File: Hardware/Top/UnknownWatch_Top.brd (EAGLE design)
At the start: 38 x 38 mm, 49 parts, among them U2 NRF52832_MODULE_MDBT42, U4 PCF8523

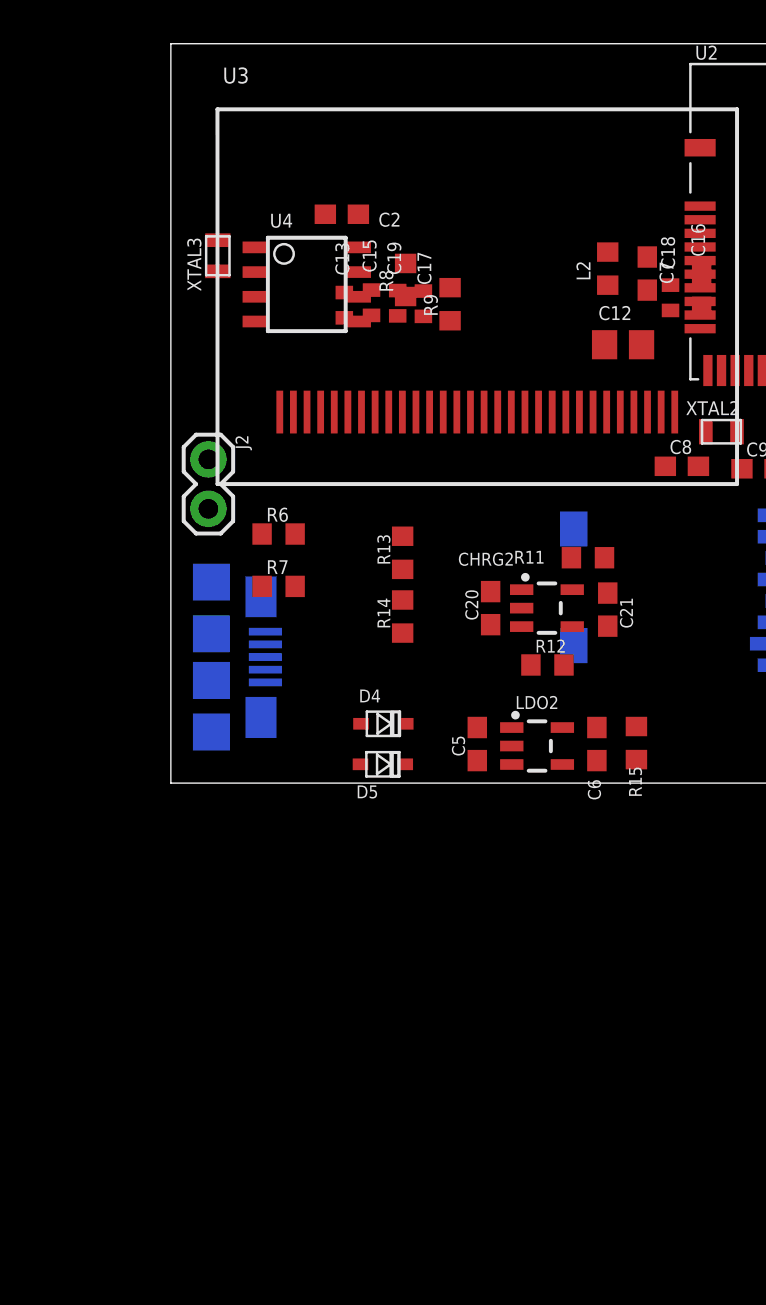
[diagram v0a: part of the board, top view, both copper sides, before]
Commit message: Adde Buttons
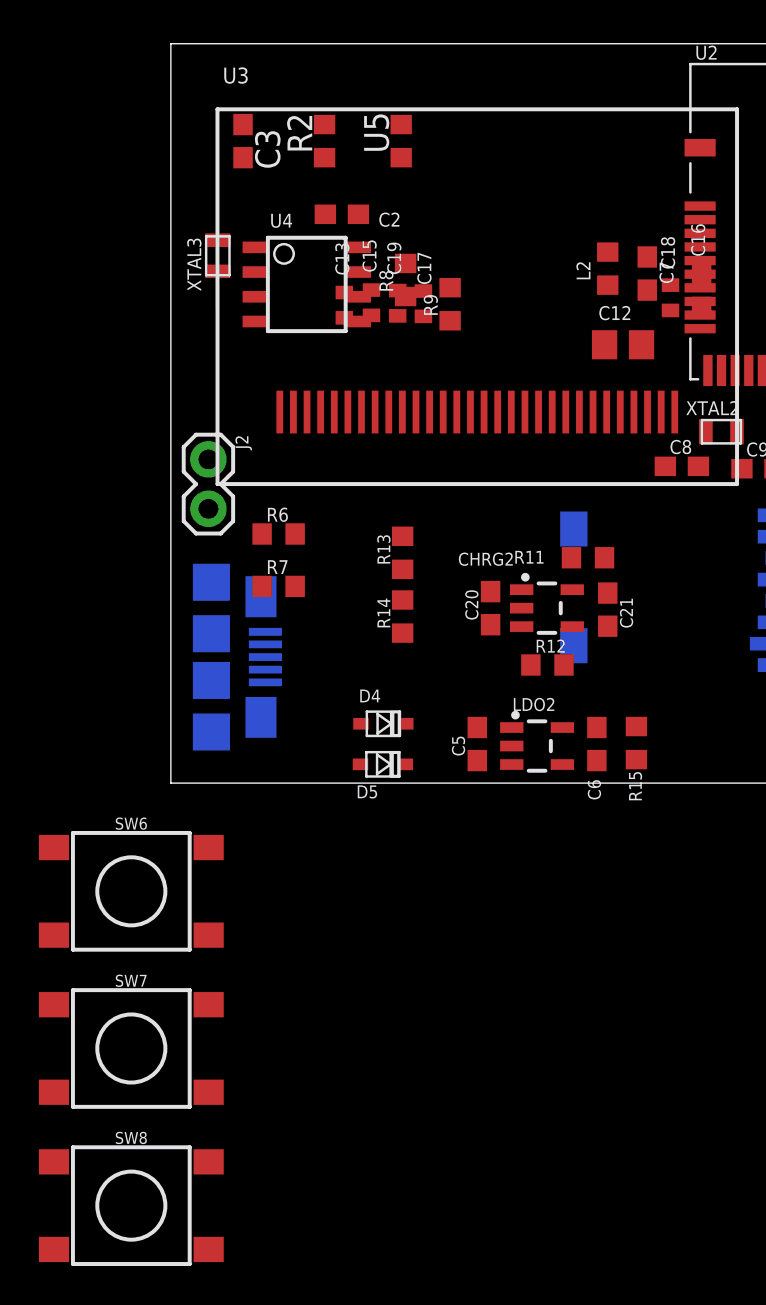
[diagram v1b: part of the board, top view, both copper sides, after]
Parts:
- added C3: 2.2u, LinnesLab-Passives:C0603
- added R2: 10k, LinnesLab-Passives:R0603
- added SW6, SW7, SW8: SWITCH.MOM, LinnesLab-Switches:TACTILE_SWITCH_SMD_6.2MM_TALL
- added U5: PHOTOTRANSISTOR, LinnesLab-Sensors:R0603
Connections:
- new net N$16: SW6.B1, SW6.B2
- new net N$18: SW6.A1
- new net OUTPUT: C3.1, R2.2, U5.2
- net 3.3V: now also U5.1
- net GND: now also C3.2, R2.1
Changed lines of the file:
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@@
 <drawing>
 <settings>
-<setting alwaysvectorfont="yes"/>
+<setting alwaysvectorfont="no"/>
 <setting verticaltext="up"/>
 </settings>
@@
 </element>
 <element name="LDO2" library="LinnesLab-Power" package="SOT23-5" value="MIC5504" x="18.8214" y="1.905" smashed="yes" rot="R270">
-<attribute name="NAME" x="18.8214" y="3.81" size="0.6604" layer="25" ratio="20" align="bottom-center"/>
+<attribute name="NAME" x="18.669" y="3.7084" size="0.6604" layer="25" ratio="20" align="bottom-center"/>
 <attribute name="VALUE" x="18.8214" y="-0.635" size="0.6604" layer="27" ratio="20" align="bottom-center"/>
 </element>
@@
 </element>
 <element name="R15" library="LinnesLab-Passives" package="R0603" package3d_urn="urn:adsk.eagle:package:15661944/2" value="100k" x="23.9268" y="2.0574" smashed="yes" rot="R90">
-<attribute name="NAME" x="24.2062" y="-0.7366" size="0.6604" layer="25" rot="R90"/>
+<attribute name="NAME" x="24.2062" y="-0.9652" size="0.6604" layer="25" rot="R90"/>
 <attribute name="VALUE" x="25.8318" y="1.4224" size="1.27" layer="27" rot="R90"/>
 </element>
@@
 <attribute name="NAME" x="5.08" y="28.5496" size="0.7112" layer="25"/>
 <attribute name="VALUE" x="5.08" y="22.0726" size="0.7112" layer="27"/>
+</element>
+<element name="U5" library="LinnesLab-Sensors" package="R0603" package3d_urn="urn:adsk.eagle:package:17881375/3" value="PHOTOTRANSISTOR" x="11.8364" y="32.9946" smashed="yes" rot="R90">
+<attribute name="NAME" x="11.2014" y="32.3596" size="1.27" layer="25" rot="R90"/>
+<attribute name="VALUE" x="13.7414" y="32.3596" size="1.27" layer="27" rot="R90"/>
+</element>
+<element name="R2" library="LinnesLab-Passives" package="R0603" package3d_urn="urn:adsk.eagle:package:15661944/2" value="10k" x="7.8994" y="32.9946" smashed="yes" rot="R90">
+<attribute name="NAME" x="7.2644" y="32.3596" size="1.27" layer="25" rot="R90"/>
+<attribute name="VALUE" x="9.8044" y="32.3596" size="1.27" layer="27" rot="R90"/>
+</element>
+<element name="C3" library="LinnesLab-Passives" package="C0603" package3d_urn="urn:adsk.eagle:package:15661989/2" value="2.2u" x="3.7084" y="32.9946" smashed="yes" rot="R270">
+<attribute name="NAME" x="4.3434" y="33.6296" size="1.27" layer="25" rot="R270"/>
+<attribute name="VALUE" x="1.8034" y="33.6296" size="1.27" layer="27" rot="R270"/>
+</element>
+<element name="SW6" library="LinnesLab-Switches" package="TACTILE_SWITCH_SMD_6.2MM_TALL" value="SWITCH.MOM" x="-2.032" y="-5.5626" smashed="yes">
+<attribute name="NAME" x="-2.032" y="-2.3876" size="0.6096" layer="25" ratio="20" align="bottom-center"/>
+<attribute name="VALUE" x="-2.032" y="-8.7376" size="0.6096" layer="27" ratio="20" align="top-center"/>
+</element>
+<element name="SW7" library="LinnesLab-Switches" package="TACTILE_SWITCH_SMD_6.2MM_TALL" value="SWITCH.MOM" x="-2.032" y="-13.6398" smashed="yes">
+<attribute name="NAME" x="-2.032" y="-10.4648" size="0.6096" layer="25" ratio="20" align="bottom-center"/>
+<attribute name="VALUE" x="-2.032" y="-16.8148" size="0.6096" layer="27" ratio="20" align="top-center"/>
+</element>
+<element name="SW8" library="LinnesLab-Switches" package="TACTILE_SWITCH_SMD_6.2MM_TALL" value="SWITCH.MOM" x="-2.032" y="-21.717" smashed="yes">
+<attribute name="NAME" x="-2.032" y="-18.542" size="0.6096" layer="25" ratio="20" align="bottom-center"/>
+<attribute name="VALUE" x="-2.032" y="-24.892" size="0.6096" layer="27" ratio="20" align="top-center"/>
 </element>
 </elements>
@@
 <contactref element="C2" pad="2"/>
 <contactref element="U4" pad="4"/>
+<contactref element="C3" pad="2"/>
+<contactref element="R2" pad="1"/>
 <wire x1="42.9006" y1="32.1564" x2="47.1426" y2="31.9654" width="0" layer="19" extent="1-1"/>
 <wire x1="41.6306" y1="32.1564" x2="42.9006" y2="32.1564" width="0" layer="19" extent="1-1"/>
@@
 <wire x1="11.6586" y1="25.3134" x2="12.9794" y2="25.288" width="0" layer="19" extent="1-1"/>
 <wire x1="7.9384" y1="29.2354" x2="11.6586" y2="25.3134" width="0" layer="19" extent="1-1"/>
+<wire x1="7.8994" y1="32.1446" x2="7.9384" y2="29.2354" width="0" layer="19" extent="1-1"/>
+<wire x1="3.7084" y1="32.1446" x2="7.8994" y2="32.1446" width="0" layer="19" extent="1-1"/>
 <wire x1="27.2008" y1="32.6544" x2="27.2796" y2="26.1484" width="0" layer="19" extent="1-1"/>
 <wire x1="17.5213" y1="1.905" x2="18.0293" y2="8.9916" width="0" layer="19" extent="1-1"/>
@@
 <contactref element="R9" pad="2"/>
 <contactref element="U4" pad="8"/>
+<contactref element="U5" pad="1"/>
 <wire x1="45.3136" y1="20.5604" x2="44.1706" y2="32.1564" width="0" layer="19" extent="1-1"/>
 <wire x1="47.7266" y1="20.7334" x2="45.3136" y2="20.5604" width="0" layer="19" extent="1-1"/>
@@
 <wire x1="9.635" y1="27.5336" x2="12.065" y2="26.7072" width="0" layer="19" extent="1-1"/>
 <wire x1="9.6384" y1="29.2354" x2="9.635" y2="27.5336" width="0" layer="19" extent="1-1"/>
+<wire x1="11.8364" y1="32.1446" x2="9.6384" y2="29.2354" width="0" layer="19" extent="1-1"/>
 <wire x1="11.198" y1="19.0692" x2="11.6586" y2="24.0134" width="0" layer="19" extent="1-1"/>
 <wire x1="9.098" y1="19.0692" x2="11.198" y2="19.0692" width="0" layer="19" extent="1-1"/>
@@
 <contactref element="U4" pad="3"/>
 </signal>
+<signal name="OUTPUT">
+<contactref element="U5" pad="2"/>
+<contactref element="R2" pad="2"/>
+<contactref element="C3" pad="1"/>
+<wire x1="7.8994" y1="33.8446" x2="11.8364" y2="33.8446" width="0" layer="19" extent="1-1"/>
+<wire x1="3.7084" y1="33.8446" x2="7.8994" y2="33.8446" width="0" layer="19" extent="1-1"/>
+</signal>
+<signal name="N$16">
+<contactref element="SW6" pad="B1"/>
+<contactref element="SW6" pad="B2"/>
+<wire x1="1.943" y1="-3.3126" x2="-6.007" y2="-3.3126" width="0" layer="19" extent="1-1"/>
+</signal>
+<signal name="N$18">
+<contactref element="SW6" pad="A1"/>
+</signal>
 </signals>

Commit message: Added a comment of all the pins that need to be kept track of.
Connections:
- net VBATT renamed VBAT
- net GND: now also USB2.S1, USB2.S2, USB2.S3, USB2.S4, USB2.S5, USB2.S6
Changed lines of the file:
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@@
 <contactref element="C3" pad="2"/>
 <contactref element="R2" pad="1"/>
+<contactref element="USB2" pad="S6"/>
+<contactref element="USB2" pad="S5"/>
+<contactref element="USB2" pad="S1"/>
+<contactref element="USB2" pad="S4"/>
+<contactref element="USB2" pad="S2"/>
+<contactref element="USB2" pad="S3"/>
 <wire x1="42.9006" y1="32.1564" x2="47.1426" y2="31.9654" width="0" layer="19" extent="1-1"/>
 <wire x1="41.6306" y1="32.1564" x2="42.9006" y2="32.1564" width="0" layer="19" extent="1-1"/>
@@
 <wire x1="11.9126" y1="7.7098" x2="16.4338" y2="9.8416" width="0" layer="19" extent="1-1"/>
 <wire x1="6.3872" y1="10.1092" x2="11.9126" y2="7.7098" width="0" layer="19" extent="1-1"/>
-<wire x1="4.8578" y1="7.777" x2="6.3872" y2="10.1092" width="0" layer="19" extent="1-16"/>
+<wire x1="4.6328" y1="9.577" x2="6.3872" y2="10.1092" width="0" layer="19" extent="1-16"/>
+<wire x1="4.8578" y1="7.777" x2="4.6328" y2="9.577" width="0" layer="19" extent="16-16"/>
+<wire x1="2.0828" y1="10.327" x2="4.6328" y2="9.577" width="0" layer="19" extent="16-16"/>
+<wire x1="2.0828" y1="7.677" x2="2.0828" y2="10.327" width="0" layer="19" extent="16-16"/>
+<wire x1="2.0828" y1="5.277" x2="2.0828" y2="7.677" width="0" layer="19" extent="16-16"/>
+<wire x1="2.0828" y1="2.627" x2="2.0828" y2="5.277" width="0" layer="19" extent="16-16"/>
+<wire x1="4.6328" y1="3.377" x2="2.0828" y2="2.627" width="0" layer="19" extent="16-16"/>
 <wire x1="4.6872" y1="12.8016" x2="6.3872" y2="10.1092" width="0" layer="19" extent="1-1"/>
 <wire x1="1.9304" y1="16.637" x2="4.6872" y2="12.8016" width="0" layer="19" extent="1-1"/>
@@
 <wire x1="2.413" y1="27.9018" x2="4.335" y2="27.5336" width="0" layer="19" extent="1-1"/>
 </signal>
-<signal name="VBATT">
-<contactref element="U4" pad="3"/>
-</signal>
 <signal name="OUTPUT">
 <contactref element="U5" pad="2"/>
@@
 <contactref element="SW6" pad="A1"/>
 </signal>
+<signal name="VBAT">
+<contactref element="U4" pad="3"/>
+</signal>
 </signals>

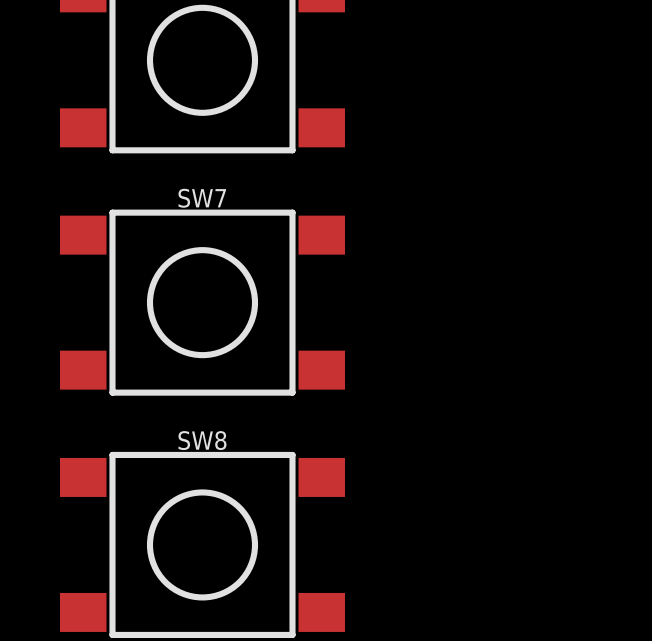
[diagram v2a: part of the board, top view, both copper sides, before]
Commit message: Made changes to buttons
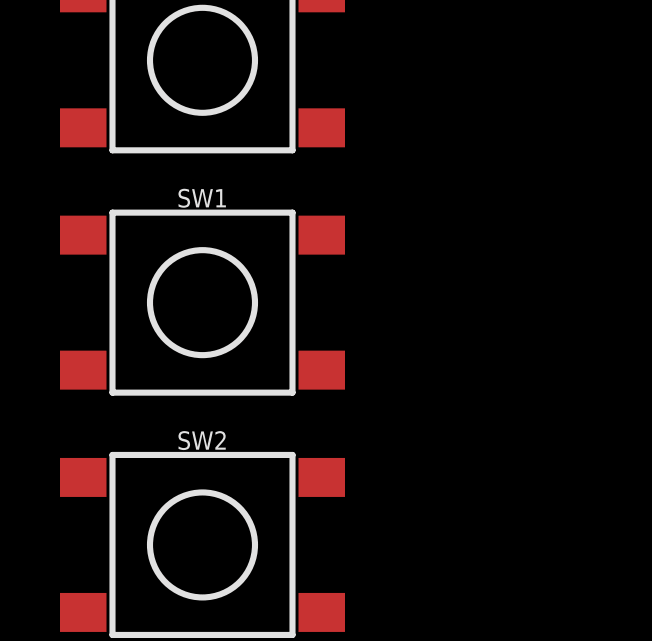
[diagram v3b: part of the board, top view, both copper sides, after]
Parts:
- renumbered SW7 to SW1, SW8 to SW2
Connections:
- removed net N$16: SW6.B1, SW6.B2
- removed net N$18: SW6.A1
- new net SW1: SW1.A1, SW2.A1, SW6.A1
- net GND: now also SW1.B1, SW1.B2, SW2.B1, SW2.B2, SW6.B1, SW6.B2
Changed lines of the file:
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@@
 <attribute name="VALUE" x="-2.032" y="-8.7376" size="0.6096" layer="27" ratio="20" align="top-center"/>
 </element>
-<element name="SW7" library="LinnesLab-Switches" package="TACTILE_SWITCH_SMD_6.2MM_TALL" value="SWITCH.MOM" x="-2.032" y="-13.6398" smashed="yes">
+<element name="SW1" library="LinnesLab-Switches" package="TACTILE_SWITCH_SMD_6.2MM_TALL" value="SWITCH.MOM" x="-2.032" y="-13.6398" smashed="yes">
 <attribute name="NAME" x="-2.032" y="-10.4648" size="0.6096" layer="25" ratio="20" align="bottom-center"/>
 <attribute name="VALUE" x="-2.032" y="-16.8148" size="0.6096" layer="27" ratio="20" align="top-center"/>
 </element>
-<element name="SW8" library="LinnesLab-Switches" package="TACTILE_SWITCH_SMD_6.2MM_TALL" value="SWITCH.MOM" x="-2.032" y="-21.717" smashed="yes">
+<element name="SW2" library="LinnesLab-Switches" package="TACTILE_SWITCH_SMD_6.2MM_TALL" value="SWITCH.MOM" x="-2.032" y="-21.717" smashed="yes">
 <attribute name="NAME" x="-2.032" y="-18.542" size="0.6096" layer="25" ratio="20" align="bottom-center"/>
 <attribute name="VALUE" x="-2.032" y="-24.892" size="0.6096" layer="27" ratio="20" align="top-center"/>
@@
 <contactref element="USB2" pad="S2"/>
 <contactref element="USB2" pad="S3"/>
+<contactref element="SW6" pad="B1"/>
+<contactref element="SW6" pad="B2"/>
+<contactref element="SW1" pad="B1"/>
+<contactref element="SW1" pad="B2"/>
+<contactref element="SW2" pad="B1"/>
+<contactref element="SW2" pad="B2"/>
 <wire x1="42.9006" y1="32.1564" x2="47.1426" y2="31.9654" width="0" layer="19" extent="1-1"/>
 <wire x1="41.6306" y1="32.1564" x2="42.9006" y2="32.1564" width="0" layer="19" extent="1-1"/>
@@
 <wire x1="11.898" y1="19.0692" x2="10.498" y2="19.0692" width="0" layer="19" extent="1-1"/>
 <wire x1="13.298" y1="19.0692" x2="11.898" y2="19.0692" width="0" layer="19" extent="1-1"/>
+<wire x1="1.943" y1="-3.3126" x2="2.0828" y2="2.627" width="0" layer="19" extent="1-16"/>
 <wire x1="12.9794" y1="25.288" x2="13.298" y2="19.0692" width="0" layer="19" extent="1-1"/>
 <wire x1="11.6586" y1="25.3134" x2="12.9794" y2="25.288" width="0" layer="19" extent="1-1"/>
@@
 <wire x1="21.8948" y1="1.1566" x2="17.5213" y2="1.905" width="0" layer="19" extent="1-1"/>
 <wire x1="23.9268" y1="1.2074" x2="21.8948" y2="1.1566" width="0" layer="19" extent="1-1"/>
+<wire x1="-6.007" y1="-3.3126" x2="1.943" y2="-3.3126" width="0" layer="19" extent="1-1"/>
+<wire x1="-6.007" y1="-11.3898" x2="-6.007" y2="-3.3126" width="0" layer="19" extent="1-1"/>
+<wire x1="1.943" y1="-11.3898" x2="-6.007" y2="-11.3898" width="0" layer="19" extent="1-1"/>
+<wire x1="-6.007" y1="-19.467" x2="-6.007" y2="-11.3898" width="0" layer="19" extent="1-1"/>
+<wire x1="1.943" y1="-19.467" x2="-6.007" y2="-19.467" width="0" layer="19" extent="1-1"/>
 <wire x1="34.7092" y1="1.4622" x2="31.3092" y2="11.5622" width="0" layer="19" extent="16-16"/>
 </signal>
@@
 <wire x1="3.7084" y1="33.8446" x2="7.8994" y2="33.8446" width="0" layer="19" extent="1-1"/>
 </signal>
-<signal name="N$16">
-<contactref element="SW6" pad="B1"/>
-<contactref element="SW6" pad="B2"/>
-<wire x1="1.943" y1="-3.3126" x2="-6.007" y2="-3.3126" width="0" layer="19" extent="1-1"/>
-</signal>
-<signal name="N$18">
+<signal name="SW1">
 <contactref element="SW6" pad="A1"/>
+<contactref element="SW1" pad="A1"/>
+<contactref element="SW2" pad="A1"/>
+<wire x1="-6.007" y1="-15.8898" x2="-6.007" y2="-23.967" width="0" layer="19" extent="1-1"/>
+<wire x1="-6.007" y1="-7.8126" x2="-6.007" y2="-15.8898" width="0" layer="19" extent="1-1"/>
 </signal>
 <signal name="VBAT">

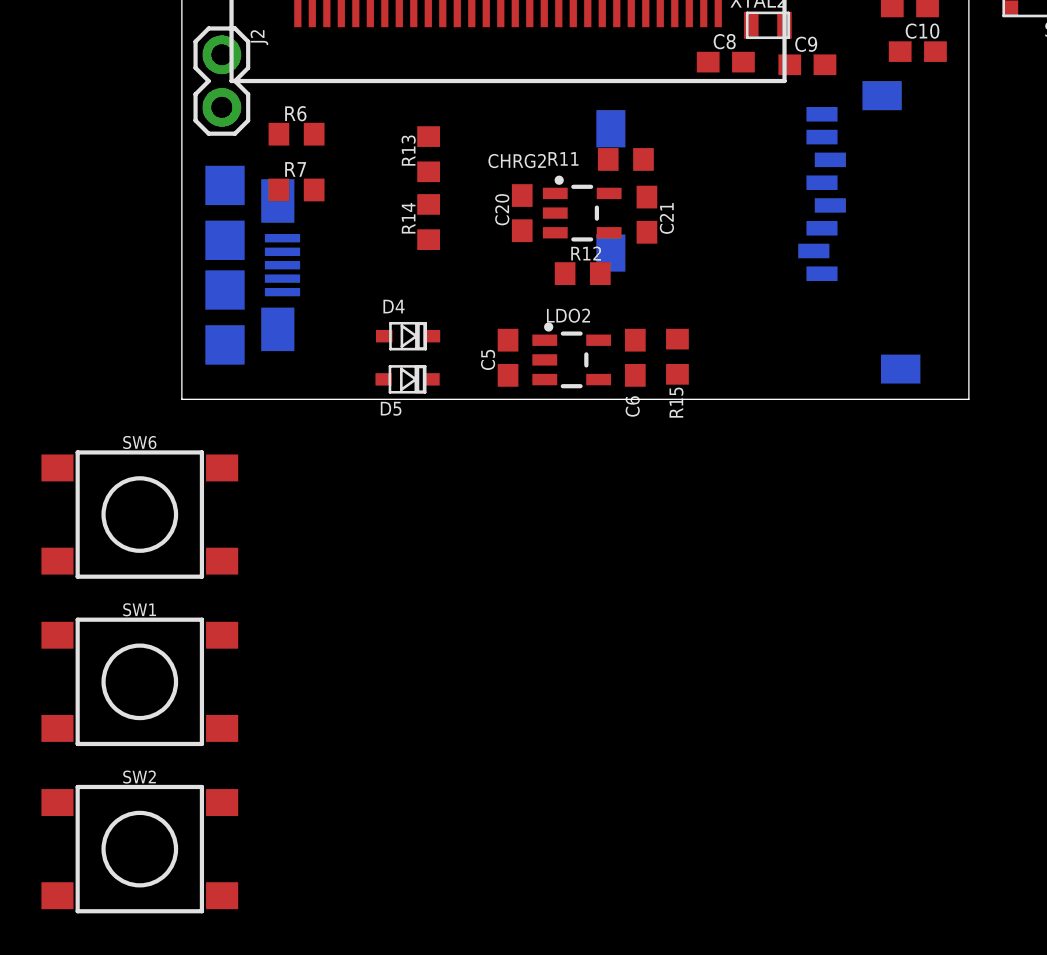
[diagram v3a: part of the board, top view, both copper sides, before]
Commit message: Deleted a button
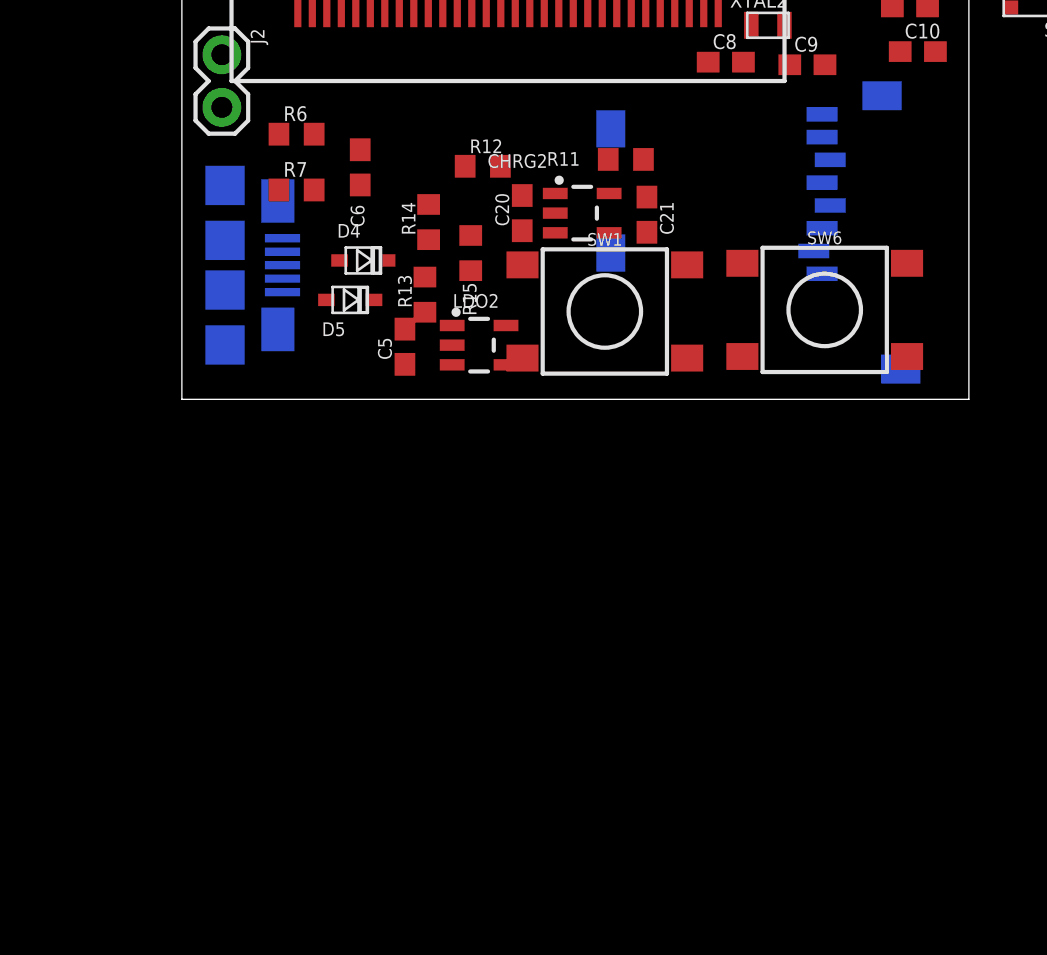
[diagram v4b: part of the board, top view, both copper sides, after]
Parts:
- removed SW2: SWITCH.MOM, LinnesLab-Switches:TACTILE_SWITCH_SMD_6.2MM_TALL
- moved SW6 34.5 mm to (31.0, 4.32)
- moved SW1 28.7 mm to (20.4, 4.24)
- moved C6 16.2 mm to (8.61, 11.2)
- moved R15 11.2 mm to (13.9, 7.06)
- moved R12 7.08 mm to (14.5, 11.3)
- moved R13 6.78 mm to (11.7, 5.05)
- moved C5 5.01 mm to (10.8, 2.54)
- moved D5 4.73 mm to (8.13, 4.80)
- moved LDO2 4.53 mm to (14.4, 2.62)
- moved D4 4.25 mm to (8.76, 6.71)
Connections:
- net GND: no longer SW2.B1, SW2.B2
- net SW1: no longer SW2.A1
